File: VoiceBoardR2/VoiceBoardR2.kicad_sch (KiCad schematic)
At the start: 7 parts, among them U103 VoiceBoardConn_18P_254P, U302 TMUX4053

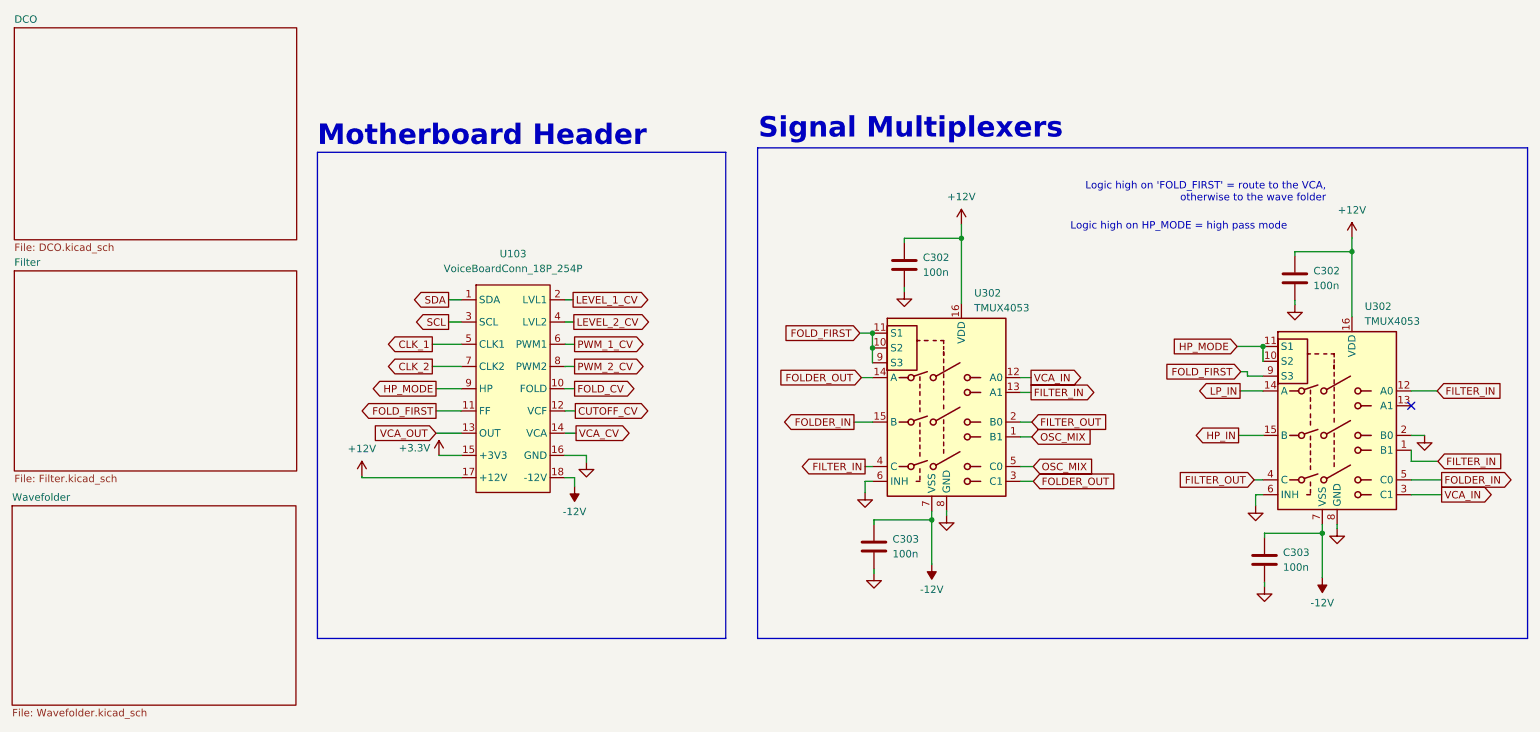
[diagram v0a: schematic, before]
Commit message: op-amp layout improved
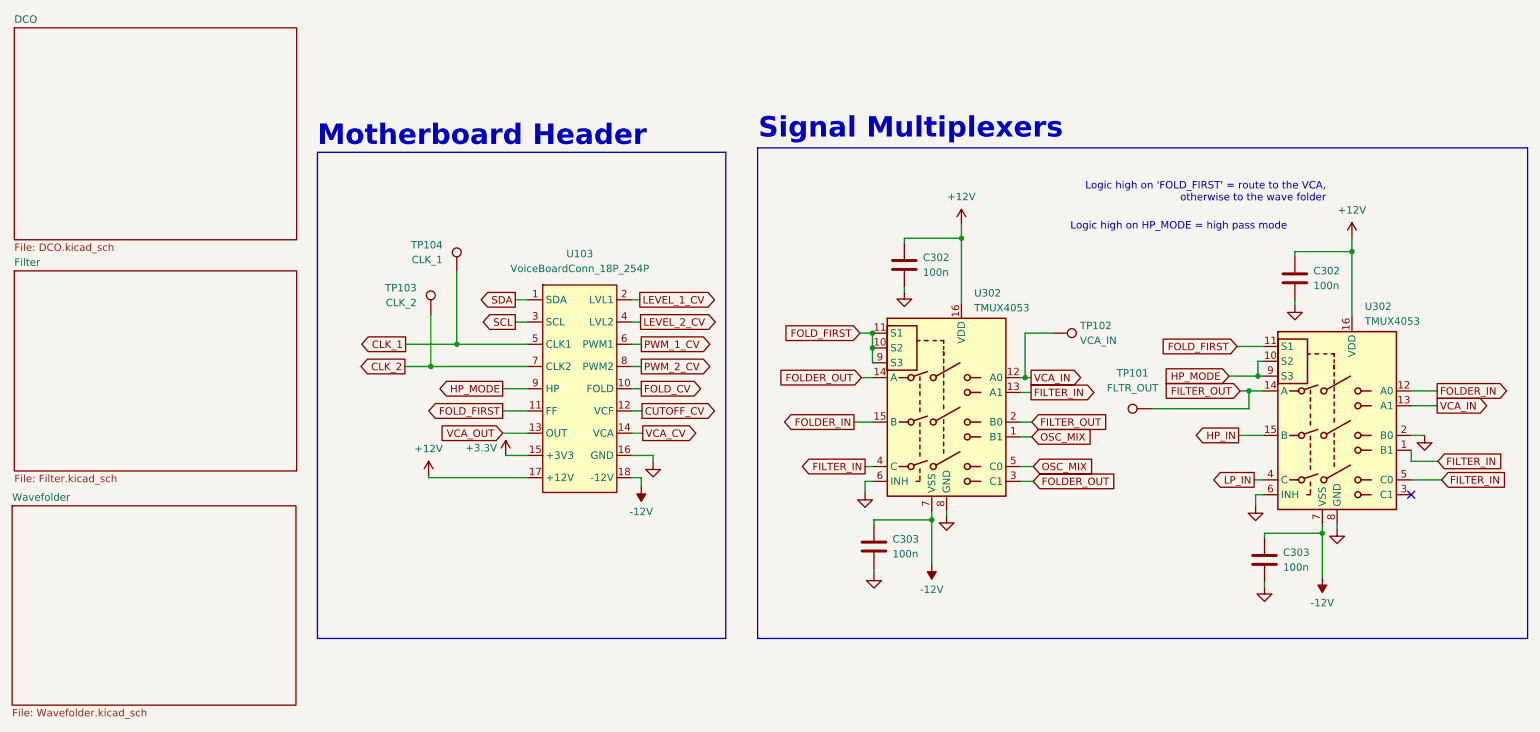
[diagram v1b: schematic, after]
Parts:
- added TP101: FLTR_OUT, TestPoint:TestPoint_Pad_D1.0mm_Value, symbol Connector:TestPoint
- added TP102: VCA_IN, TestPoint:TestPoint_Pad_D1.0mm_Value, symbol Connector:TestPoint
- added TP103: CLK_2, TestPoint:TestPoint_Pad_D1.0mm_Value, symbol Connector:TestPoint
- added TP104: CLK_1, TestPoint:TestPoint_Pad_D1.0mm_Value, symbol Connector:TestPoint
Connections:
- net CLK_1: now also TP104.1
- net CLK_2: now also TP103.1
- net FILTER_IN: now also U302.5 (C0); no longer U302.12 (A0)
- net FILTER_OUT: now also U302.14 (A), TP101.1; no longer U302.4 (C)
- net FOLDER_IN: now also U302.12 (A0); no longer U302.5 (C0)
- net FOLD_FIRST: now also U302.11 (S1); no longer U302.9 (S3)
- net HP_MODE: now also U302.9 (S3); no longer U302.11 (S1)
- net LP_IN: now also U302.4 (C); no longer U302.14 (A)
- net VCA_IN: now also U302.13 (A1), TP102.1; no longer U302.3 (C1)
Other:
- moved on the sheet: U103
